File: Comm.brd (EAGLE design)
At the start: 30 x 60 mm, 33 parts, among them SW5 THAU13-AB-R, SW6 THAU13-AB-R, SW7 TVAF06-A020B-R, SW8 TVAF06-A020B-R, U4 OPA340N, U5 DRIVER-LV8548MC-AH(SOIC10), U6 I-02247_NJM2845

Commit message: Communication unit
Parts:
- removed U$1: LITE, TWELite:LITE
- added C1: 0.1µF, rcl:C0603K
- added TWE-LITE: LITE, TWELite:LITE
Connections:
- removed net 1: U$5.P7
- removed net 2: U$5.P8
- removed net 3: U$5.P9
- removed net 4: U$5.P10
- removed net I2C_SCL: U$2.IO22
- removed net I2C_SDA: U$2.IO21
- removed net SPI_CLK: U$2.IO18
- removed net SPI_CS: U$2.IO5
- removed net SPI_MISO: U$2.IO19
- new net TWE_!PGM!: TWE-LITE.2, U$5.P8
- new net TWE_!RESET!: TWE-LITE.21, U$2.IO22, U$5.P7
- new net TWE_!RTS!: TWE-LITE.7, U$2.IO18
- new net TWE_RTX: TWE-LITE.8, U$2.IO5, U$5.P10
- new net TWE_SLEEP: TWE-LITE.27, U$2.IO23
- new net TWE_TRX: TWE-LITE.9, U$2.IO19, U$5.P9
- net GND: now also C1.2, TWE-LITE.20, TWE-LITE.28; no longer U$1.20, U$1.28
- net VCC: no longer U$1.5
- net VDD: now also C1.1, TWE-LITE.5
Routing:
- net TWE_!RESET!: track 0.00 -> 31.4 mm, vias 0 -> 1
- net GND: track 222.8 -> 248.7 mm, vias 11 -> 12
- net TWE_TRX: track 0.00 -> 18.9 mm, vias 0 -> 2
- net TWE_!PGM!: track 0.00 -> 13.4 mm, vias 0 -> 1
- net TWE_SLEEP: track 0.00 -> 11.5 mm, vias 0 -> 1
- net TWE_RTX: track 0.00 -> 9.43 mm, vias 0 -> 1
- net VDD: track 131.7 -> 124.5 mm
- net TWE_!RTS!: track 0.00 -> 4.13 mm, vias 0 -> 1

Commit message: Fix analog input pins
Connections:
- net MSENSE: now also U$2.IO32; no longer U$2.IO12
- net SW1: now also U$2.IO12; no longer U$2.IO13
- net SW2: now also U$2.IO27; no longer U$2.IO35
- net SW3: now also U$2.IO13; no longer U$2.IO14
- net SW4: now also U$2.IO14; no longer U$2.IO32
- net VSENSE: now also U$2.IO35; no longer U$2.IO27
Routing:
- net MSENSE: track 39.9 -> 50.7 mm
- net VSENSE: track 17.7 -> 27.7 mm
- net N$10: track 27.4 -> 31.8 mm
- net SW2: track 43.4 -> 39.2 mm, vias 0 -> 2
- net SW1: track 20.5 -> 24.6 mm
- net SW4: track 28.4 -> 24.6 mm, vias 1 -> 3
- net SW3: track 13.0 -> 9.40 mm
- net J2: track 23.1 -> 24.2 mm
- net J0: track 17.9 -> 18.7 mm
- net J1: track 20.9 -> 21.4 mm
- net GND: track 248.7 -> 248.5 mm, vias 12 -> 10

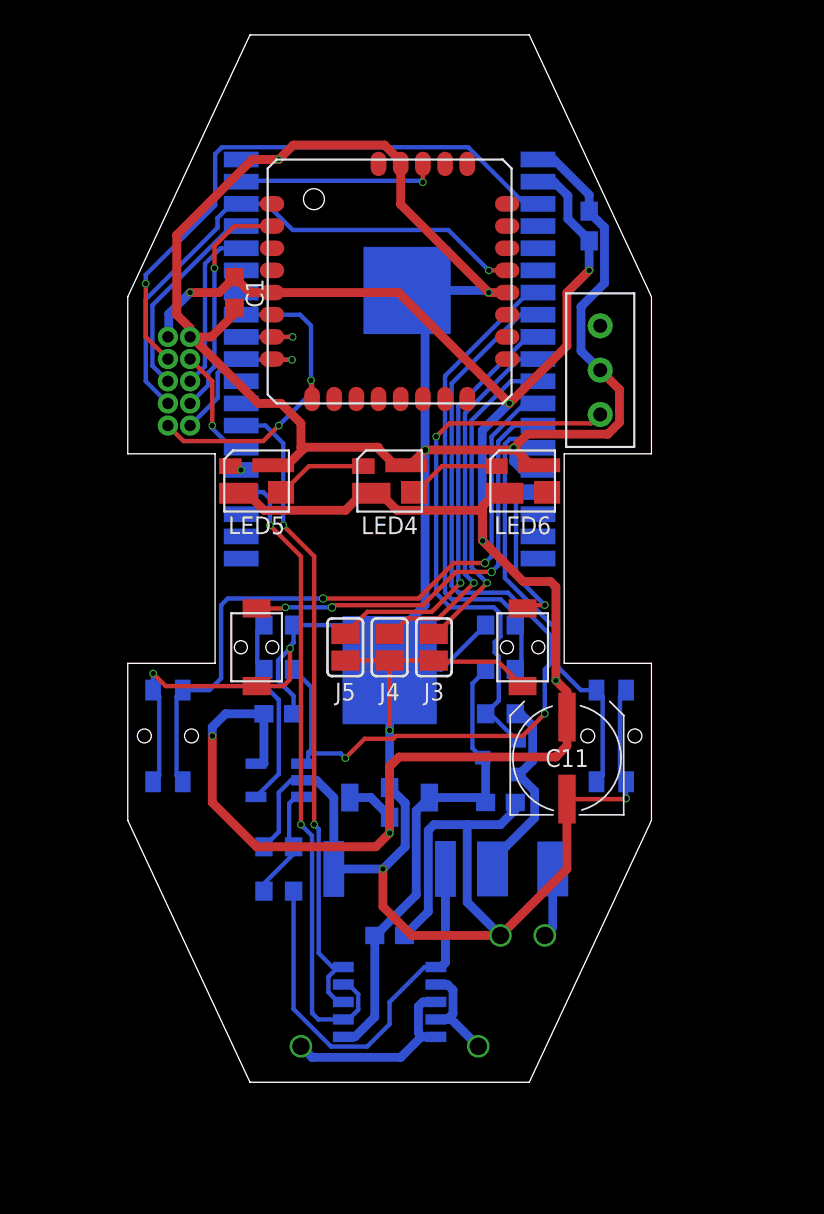
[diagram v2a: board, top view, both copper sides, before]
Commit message: reduce switch pins
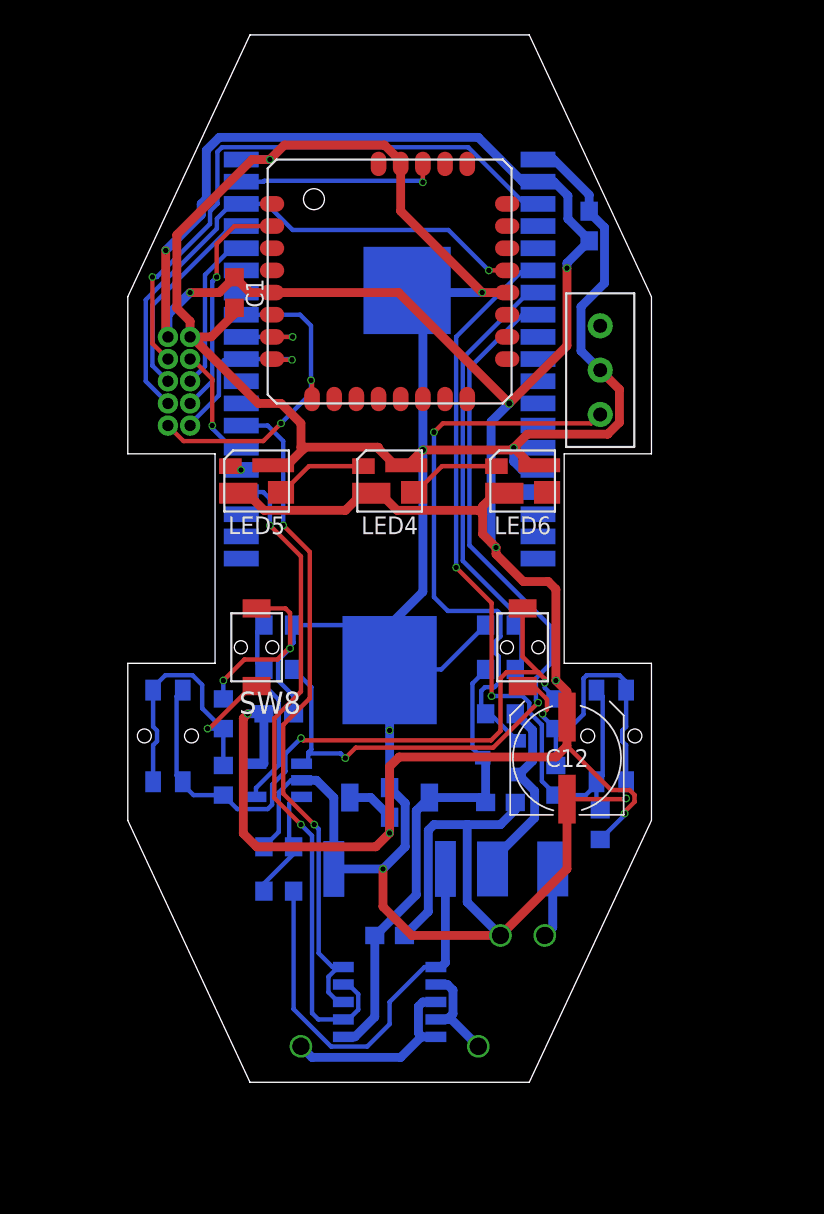
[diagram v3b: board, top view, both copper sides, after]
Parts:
- removed C7: 0.1µF, rcl:C0603
- removed J3, J4, J5: (no value), jumper:SJ
- removed R8: 1k, rcl:R0603
- removed R9: 100k, rcl:R0603
- added C13: 0.1µF, rcl:C0603
- added R18, R19: 100k, rcl:R0603
- added R20, R21, R22, R23, R24: (no value), rcl:R0603
- C10: value 2.2µF -> 0.33µF
- C11: value 220µF -> 2.2µF; device rcl:UD-6,3X7,7_NICHICON -> rcl:C0603
- C12: value 0.1µF -> 220µF; device rcl:C0603 -> rcl:UD-6,3X7,7_NICHICON
- C8: value 1µF -> 0.1µF
- C9: value 0.33µF -> 1µF
- R13: value 100k -> 1k
- moved C12 30.5 mm to (10.2, -11.4), flipped to the top
- moved C8 14.2 mm to (-6.35, -8.89), turned to 180 degrees
- moved R14 13.0 mm to (-6.35, -6.35)
- moved R13 12.7 mm to (-6.35, -3.81), turned to 0 degrees
- moved C11 10.5 mm to (0.00, -14.0), flipped to the bottom
- moved C9 9.92 mm to (0.00, -21.6), turned to 0 degrees
- moved C10 6.35 mm to (6.35, -14.0), turned to 180 degrees
- turned SW7 to 180 degrees
- turned SW8 to 180 degrees
- renumbered R10 to R15, R11 to R16, R12 to R17
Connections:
- removed net J0: J3.1, U$2.IO26
- removed net J1: J4.1, U$2.IO25
- removed net J2: J5.1, U$2.IO33
- removed net N$10: R14.1, T1.3, U$4.1
- removed net N$5: HUSE1.2, R14.2, T1.2
- removed net N$8: R8.2, R9.1, U4.4
- removed net SW1: SW6.1, SW6.2, U$2.IO12
- removed net SW2: SW5.1, SW5.2, U$2.IO27
- removed net SW3: SW7.P$1, U$2.IO13
- removed net SW4: SW8.P$1, U$2.IO14
- new net N$11: R13.2, R14.1, U4.4
- new net N$13: R19.1, T1.3, U$4.1
- new net N$16: R22.1, R23.2, SW5.1, SW5.2, SW7.P$2
- new net N$17: R21.1, R22.2, SW6.3, SW6.4, SW7.P$1
- new net N$18: R23.1, R24.2, SW5.3, SW5.4, SW8.P$1
- new net N$9: HUSE1.2, R19.2, T1.2
- new net SW: R20.1, R21.2, SW6.1, SW6.2, U$2.IO34
- net GND: now also C11.2, C12.-, C13.2, C8.2, C9.1, R18.1, R24.1; no longer C11.-, C12.2, C7.2, C8.1, C9.2, J3.2, J4.2, J5.2, R8.1, SW5.3, SW5.4, SW6.3, SW6.4, SW7.P$2
- net MSENSE: now also R14.2; no longer R9.2
- net VCC: now also C10.1, C9.2; no longer C8.2, C9.1
- net VDD: now also C11.1, C12.+, C13.1, C8.1, R20.2; no longer C10.1, C11.+, C12.1, C7.1
- net VSENSE: now also R18.2; no longer R13.2
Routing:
- net SW: track 0.00 -> 45.9 mm, vias 0 -> 2
- net SW2: track 39.2 -> 0.00 mm, vias 2 -> 0
- net N$16: track 0.00 -> 39.0 mm, vias 0 -> 2
- net VDD: track 124.5 -> 163.0 mm, vias 7 -> 9
- net N$13: track 0.00 -> 32.9 mm, vias 0 -> 1
- net N$10: track 31.8 -> 0.00 mm, vias 1 -> 0
- net GND: track 248.5 -> 219.7 mm
- net SW4: track 24.6 -> 0.00 mm, vias 3 -> 0
- net SW1: track 24.6 -> 0.00 mm
- net J2: track 24.2 -> 0.00 mm, vias 1 -> 0
- net J1: track 21.4 -> 0.00 mm, vias 1 -> 0
- net N$18: track 0.00 -> 18.8 mm, vias 0 -> 1
- net J0: track 18.7 -> 0.00 mm, vias 1 -> 0
- net N$17: track 0.00 -> 18.5 mm, vias 0 -> 1
- net N$8: track 11.6 -> 0.00 mm
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
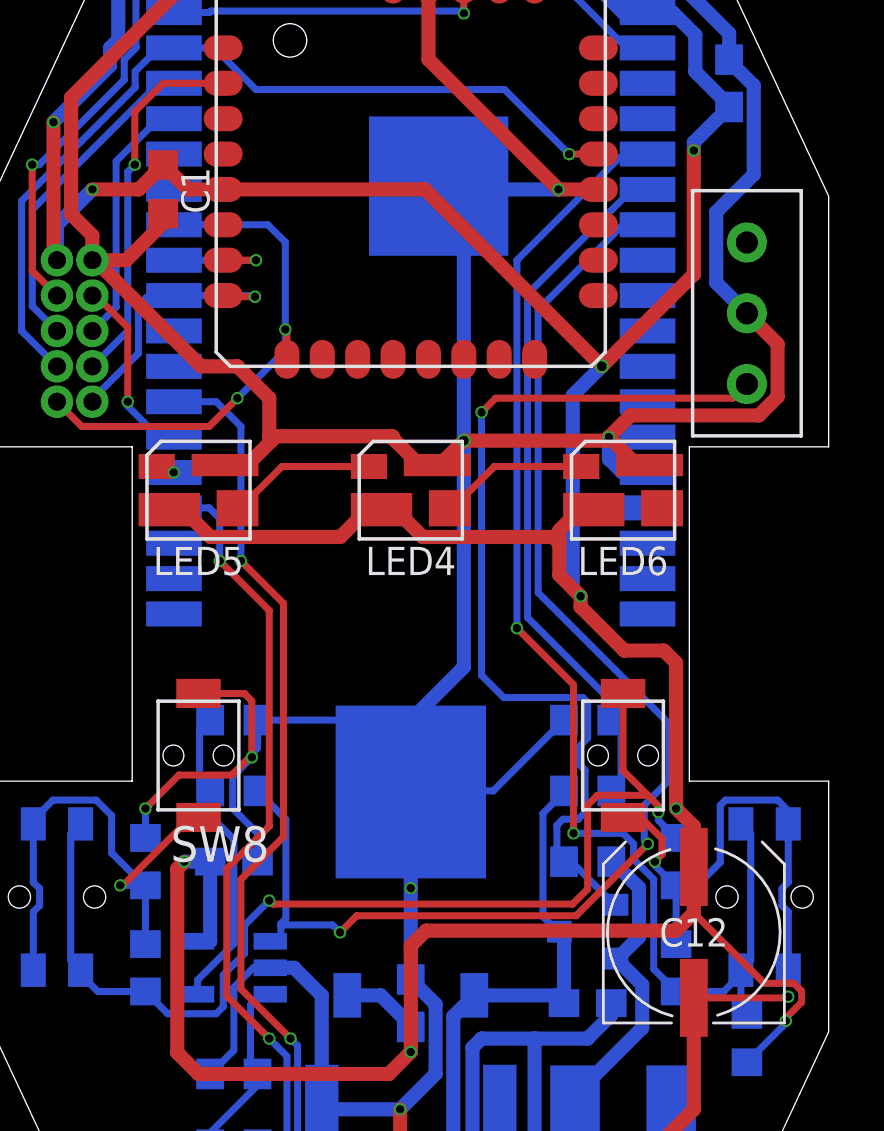
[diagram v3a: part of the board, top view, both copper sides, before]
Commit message: change parts name
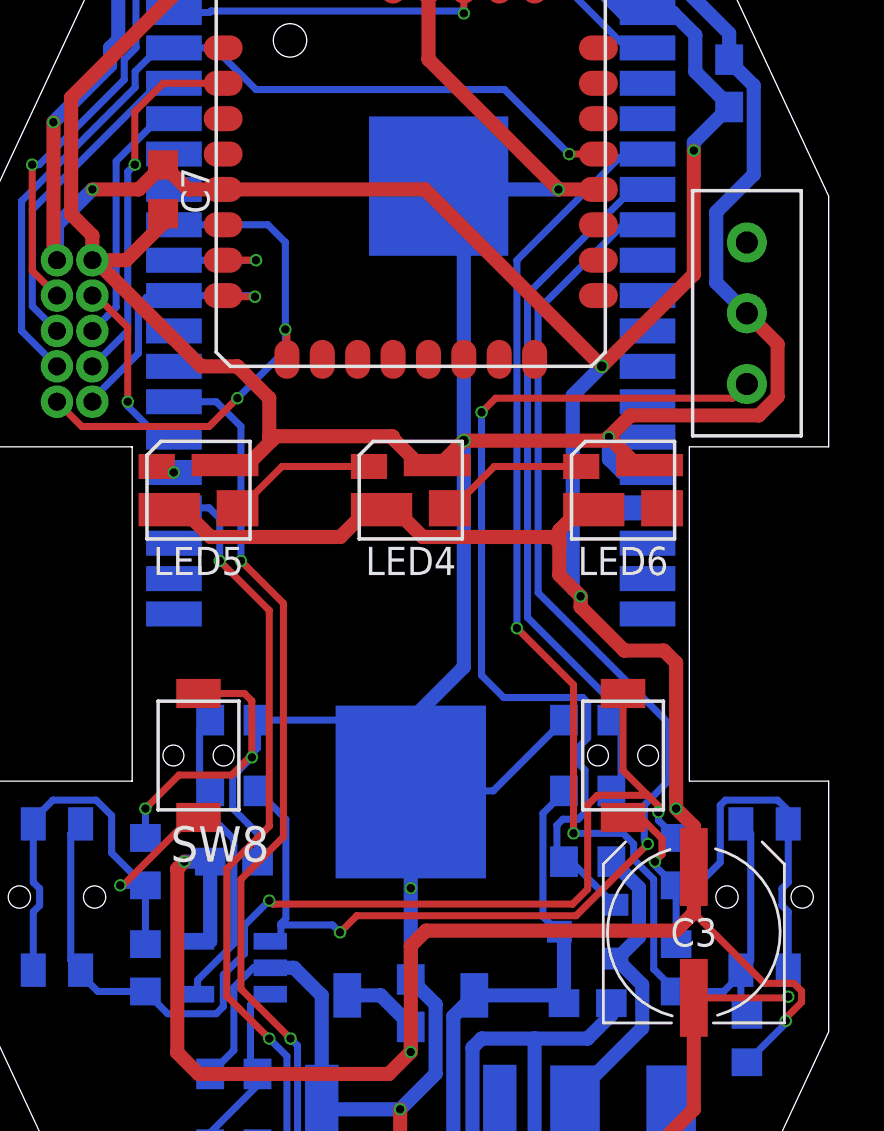
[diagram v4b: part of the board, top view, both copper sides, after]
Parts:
- removed C10: 0.33µF, rcl:C0603
- removed R24: (no value), rcl:R0603
- added C7: 0.1µF, rcl:C0603K
- added R6: 1k, rcl:R0603
- C1: value 0.1µF -> 0.33µF; device rcl:C0603K -> rcl:C0603
- R13: value 1k -> (none)
- moved C1 32.9 mm to (6.35, -14.0), flipped to the bottom, turned to 180 degrees
- moved R13 5.99 mm to (-9.53, -8.89), turned to 270 degrees
- renumbered C11 to C2, C12 to C3, C13 to C4, C8 to C6, C9 to C5, R14 to R8, R15 to R4, R16 to R7, R17 to R2, R18 to R3, R19 to R1, R20 to R9, R21 to R10, R22 to R11, R23 to R12, RS1 to R5
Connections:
- net GND: now also C7.2, R6.1; no longer C10.2, R24.1
- net N$11: now also R6.2; no longer R13.2
- net N$18: now also R13.2; no longer R24.2
- net VCC: now also C1.1; no longer C10.1
- net VDD: now also C7.1; no longer C1.1

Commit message: Format silk
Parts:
- renumbered LED4 to LED2, LED5 to LED3, LED6 to LED1, SW5 to SW2, SW6 to SW1, SW7 to SW3, SW8 to SW4

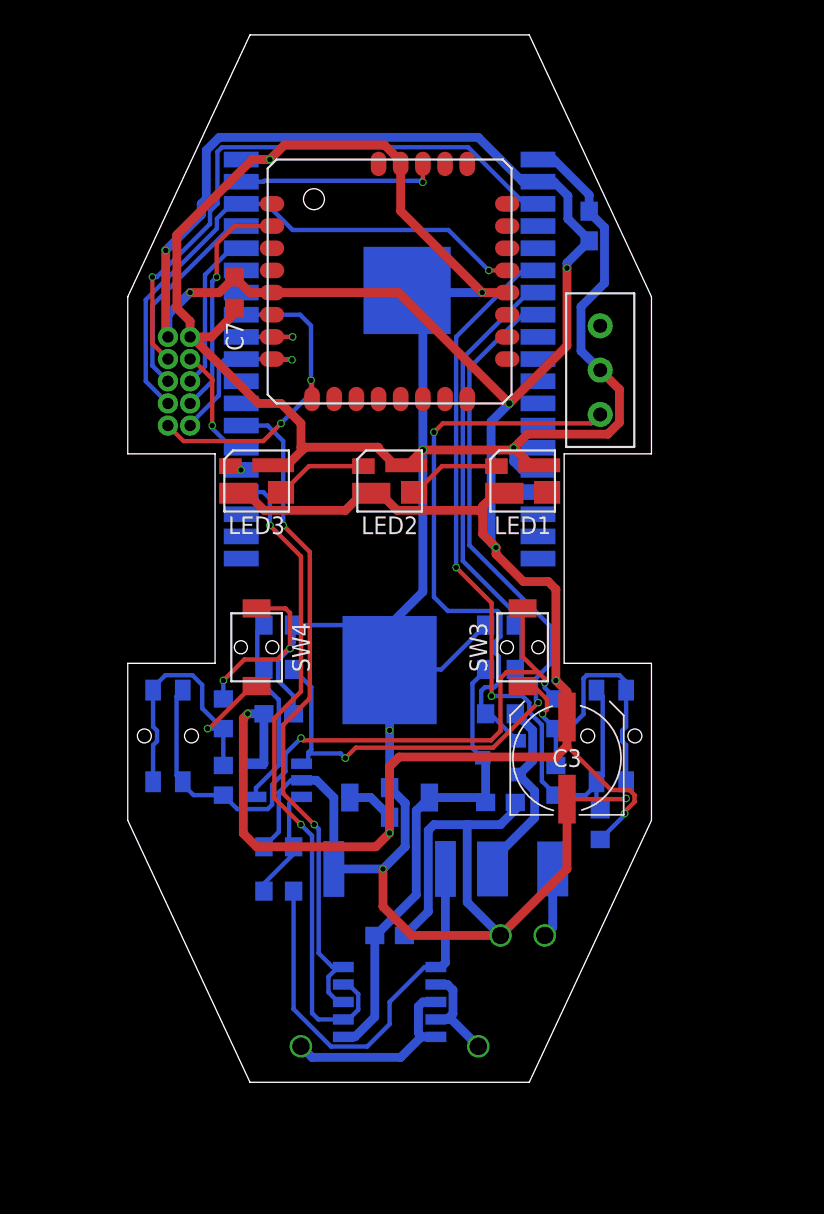
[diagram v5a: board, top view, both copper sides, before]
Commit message: Add GND plane
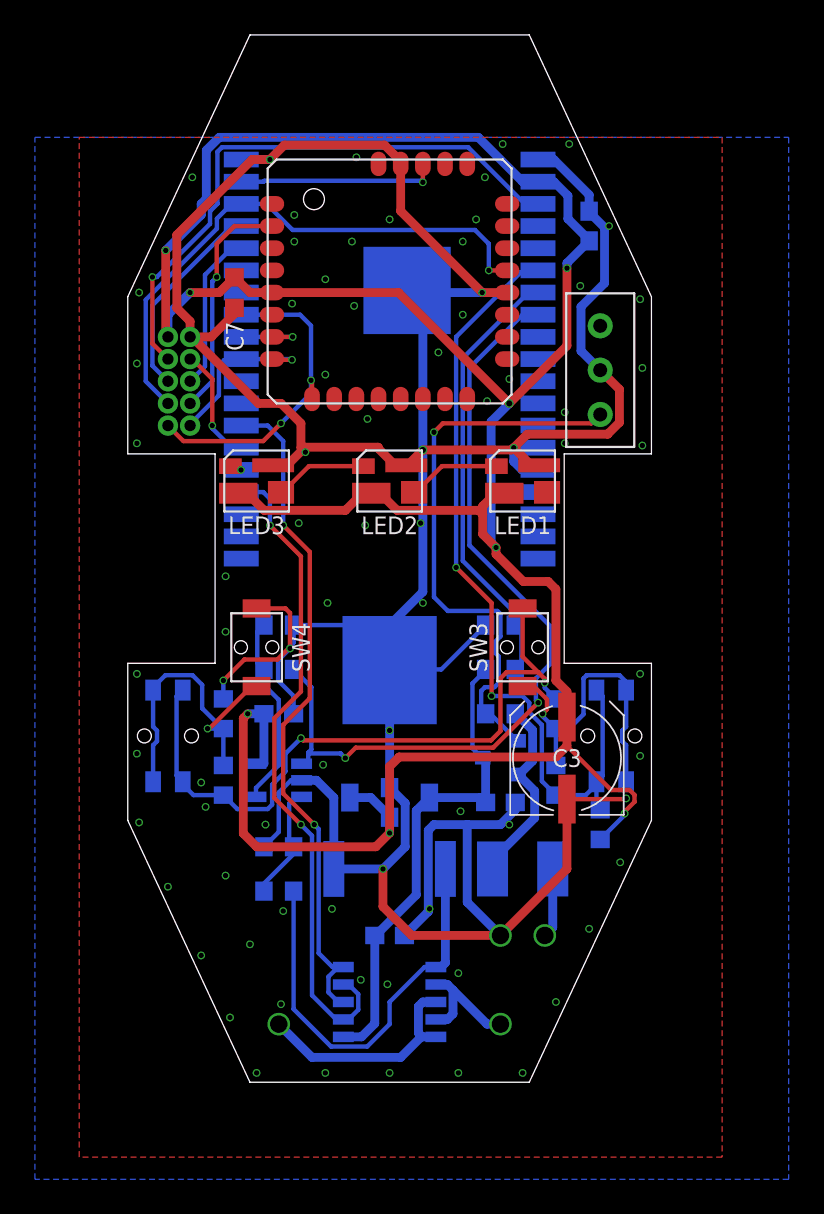
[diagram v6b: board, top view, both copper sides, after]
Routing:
- net M1: track 11.4 -> 13.2 mm
- net M2: track 5.93 -> 7.11 mm
- net TWE_!RESET!: track 31.4 -> 32.2 mm
- net MC1: track 38.5 -> 37.9 mm
- net VDD: vias 9 -> 8
- net GND: vias 10 -> 79
- added copper zone on layer 1, net GND
- added copper zone on layer 16, net GND
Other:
- board text added: "2022 WASA Rocket"
